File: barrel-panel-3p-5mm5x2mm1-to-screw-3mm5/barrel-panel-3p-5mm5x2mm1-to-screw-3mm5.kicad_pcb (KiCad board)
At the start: 2 copper layers, 1 part, among them J1 Barrel_Jack_Switch

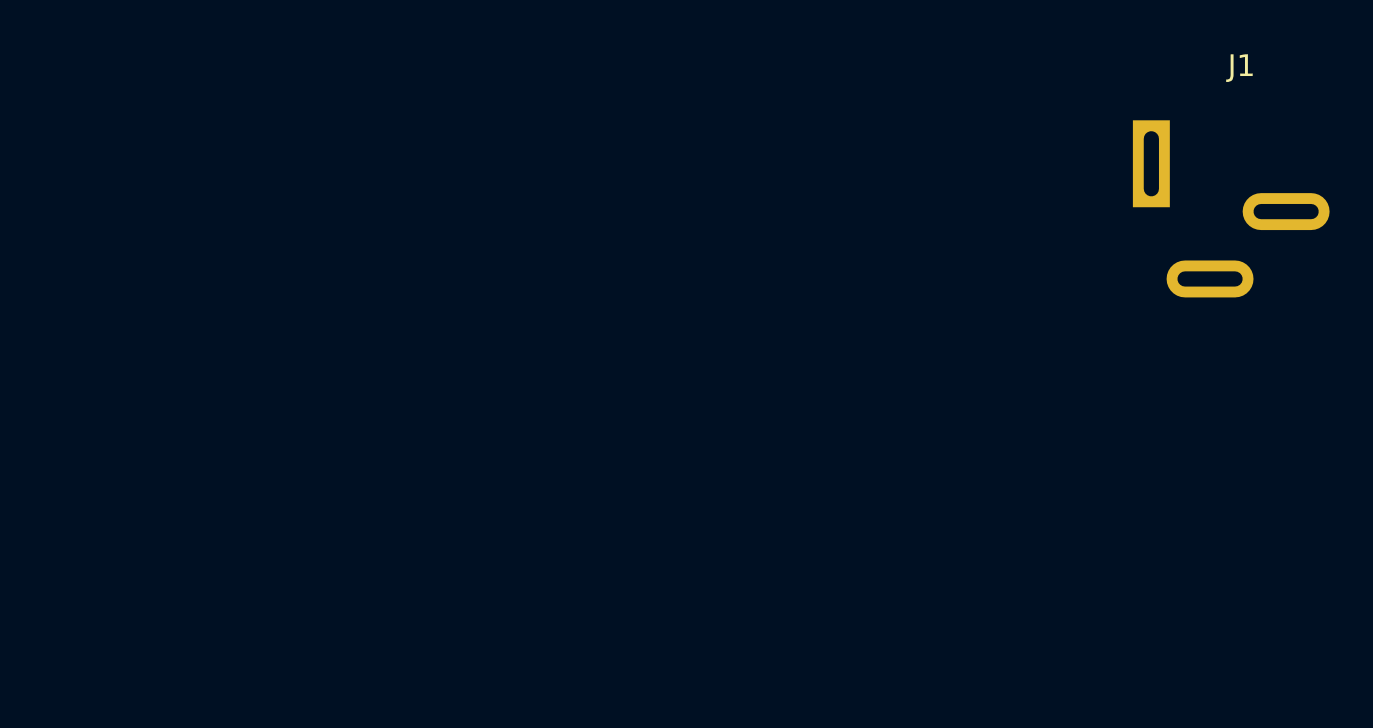
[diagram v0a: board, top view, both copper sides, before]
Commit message: footprint finished, all elements placed in board
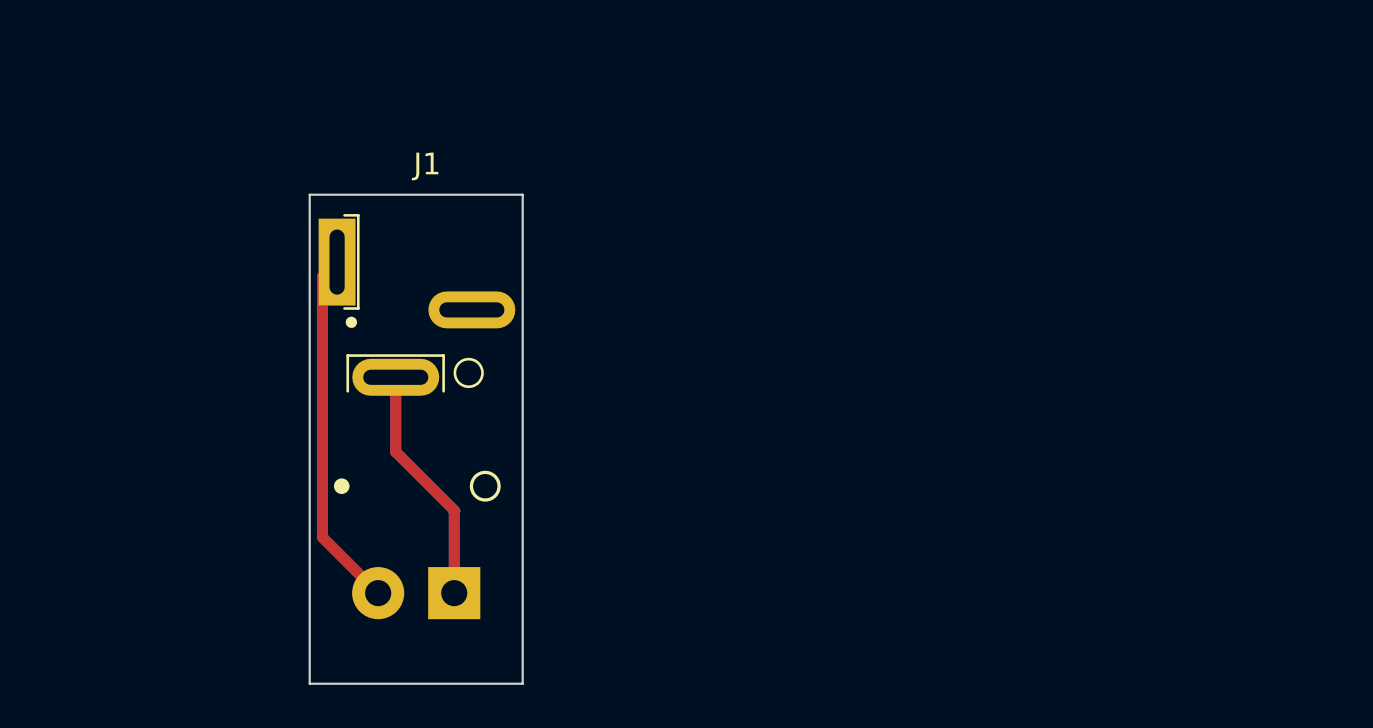
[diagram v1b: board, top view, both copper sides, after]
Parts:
- added J2: Conn_01x02_Male, TerminalBlock_4Ucon:TerminalBlock_4Ucon_1x02_P3.50mm_Horizontal, B.Cu at (106.7, 118.3)
- moved J1 37.7 mm to (105.4, 104.6)
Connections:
- J1 pad 1: unconnected-(J1-Pad1) -> Net-(J1-Pad1)
- J1 pad 2: unconnected-(J1-Pad2) -> Net-(J1-Pad2)
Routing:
- net Net-(J1-Pad1): track 0.00 -> 33.1 mm
- net Net-(J1-Pad2): track 0.00 -> 22.1 mm
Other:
- board outline added: 9.8 x 22.5 mm

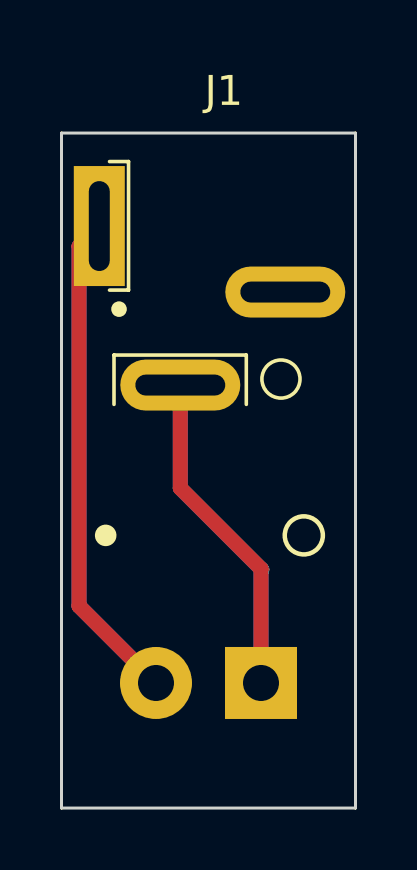
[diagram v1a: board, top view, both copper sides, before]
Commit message: shrinking pcb to let space for the nut
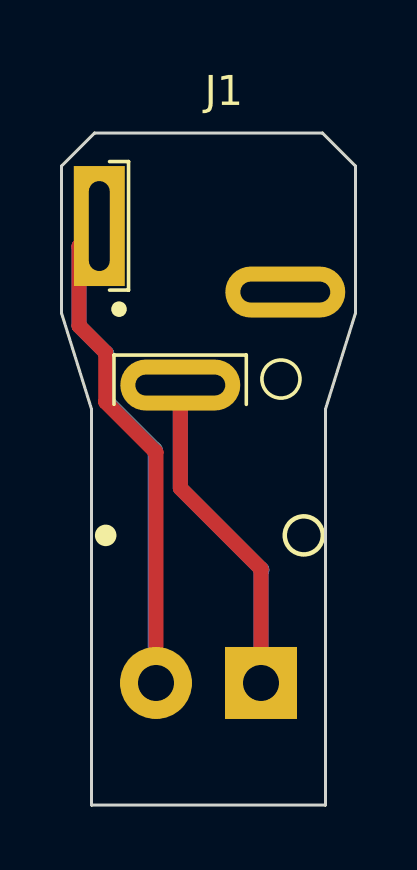
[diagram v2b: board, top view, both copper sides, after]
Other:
- board size 9.8 x 22.5 mm -> 9.8 x 22.4 mm
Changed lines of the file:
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@@
   (gr_circle (center 108.077 113.411) (end 108.585 113.03) (layer "F.SilkS") (width 0.15) (fill none))
   (gr_circle (center 101.473 113.411) (end 101.756981 113.411) (layer "F.SilkS") (width 0.15) (fill solid))
-  (gr_rect (start 100 100) (end 109.8 122.5) (layer "Edge.Cuts") (width 0.1) (fill none))
+  (gr_line (start 101.1 100) (end 108.7 100) (layer "Edge.Cuts") (width 0.1))
+  (gr_line (start 108.8 109.2) (end 109.8 106) (layer "Edge.Cuts") (width 0.1))
+  (gr_line (start 100 101.1) (end 100 106) (layer "Edge.Cuts") (width 0.1))
+  (gr_line (start 101 122.4) (end 108.8 122.4) (layer "Edge.Cuts") (width 0.1))
+  (gr_line (start 100 106) (end 101 109.2) (layer "Edge.Cuts") (width 0.1))
+  (gr_line (start 108.7 100) (end 109.8 101.1) (layer "Edge.Cuts") (width 0.1))
+  (gr_line (start 101.1 100) (end 100 101.1) (layer "Edge.Cuts") (width 0.1))
+  (gr_line (start 109.8 101.1) (end 109.8 106) (layer "Edge.Cuts") (width 0.1))
+  (gr_line (start 108.8 109.2) (end 108.8 122.4) (layer "Edge.Cuts") (width 0.1))
+  (gr_line (start 101 109.2) (end 101 122.4) (layer "Edge.Cuts") (width 0.1))
+  (segment (start 103.15 110.643) (end 103.15 118.331) (width 0.5) (layer "F.Cu") (net 1))
+  (segment (start 101.473 107.315) (end 101.473 108.966) (width 0.5) (layer "F.Cu") (net 1))
+  (segment (start 100.584 103.776) (end 100.584 106.426) (width 0.5) (layer "F.Cu") (net 1))
+  (segment (start 101.473 108.966) (end 103.15 110.643) (width 0.5) (layer "F.Cu") (net 1))
   (segment (start 101.26 103.1) (end 100.584 103.776) (width 0.5) (layer "F.Cu") (net 1))
-  (segment (start 100.584 103.776) (end 100.584 115.765) (width 0.5) (layer "F.Cu") (net 1))
-  (segment (start 100.584 115.765) (end 103.15 118.331) (width 0.5) (layer "F.Cu") (net 1))
-  (segment (start 100.584 115.765) (end 103.15 118.331) (width 0.5) (layer "B.Cu") (net 1))
-  (segment (start 100.584 103.776) (end 100.584 115.765) (width 0.5) (layer "B.Cu") (net 1))
-  (segment (start 100.584 103.776) (end 101.26 103.1) (width 0.5) (layer "B.Cu") (net 1))
+  (segment (start 100.584 106.426) (end 101.473 107.315) (width 0.5) (layer "F.Cu") (net 1))
+  (segment (start 101.51 108.938478) (end 103.124 110.552478) (width 0.5) (layer "B.Cu") (net 1))
+  (segment (start 100.584 106.426) (end 101.51 107.352) (width 0.5) (layer "B.Cu") (net 1))
+  (segment (start 101.51 107.352) (end 101.51 108.938478) (width 0.5) (layer "B.Cu") (net 1))
+  (segment (start 103.124 118.305) (end 103.15 118.331) (width 0.5) (layer "B.Cu") (net 1))
+  (segment (start 100.584 103.776) (end 100.584 106.426) (width 0.5) (layer "B.Cu") (net 1))
+  (segment (start 101.26 103.1) (end 100.584 103.776) (width 0.5) (layer "B.Cu") (net 1))
+  (segment (start 103.124 110.552478) (end 103.124 118.305) (width 0.5) (layer "B.Cu") (net 1))
   (segment (start 103.96 111.834) (end 106.65 114.524) (width 0.5) (layer "F.Cu") (net 2))
   (segment (start 103.96 108.4) (end 103.96 111.834) (width 0.5) (layer "F.Cu") (net 2))

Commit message: single board gerbers
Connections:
- J2 pad 1: Net-(J1-Pad2) -> Net-(J1-Pad1)
- J2 pad 2: Net-(J1-Pad1) -> Net-(J1-Pad2)
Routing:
- net Net-(J1-Pad1): track 33.1 -> 40.8 mm
- net Net-(J1-Pad2): track 22.1 -> 20.6 mm
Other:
- outline, holes or cut-outs redrawn
- board text added: "3.5 mm screw term"
- board text added: "DC BARREL 5.5x2.1mm"
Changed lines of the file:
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@@
       (sketchpadsonfab false)
       (subtractmaskfromsilk false)
-      (outputformat 5)
+      (outputformat 1)
       (mirror false)
-      (drillshape 2)
+      (drillshape 0)
       (scaleselection 1)
       (outputdirectory "gerber/single/")
@@
       (net 2 "Net-(J1-Pad2)") (pintype "passive"))
     (pad "3" thru_hole oval (at 2.05 0.7 90) (size 1.7 4) (drill oval 0.7 3) (layers *.Cu *.Mask)
-      (net 3 "unconnected-(J1-Pad3)") (pintype "passive"))
+      (net 3 "unconnected-(J1-Pad3)") (pintype "passive+no_connect"))
     (model "${KICAD6_3DMODEL_DIR}/Connector_BarrelJack.3dshapes/BarrelJack_Kycon_KLDX-0202-xC_Horizontal.wrl"
       (offset (xyz 0 0 0))
@@
     (property "Sheetname" "")
     (attr through_hole)
-    (fp_text reference "J2" (at 2.002 4.92) (layer "B.SilkS")
+    (fp_text reference "J2" (at 1.748 4.92) (layer "B.SilkS")
       (effects (font (size 1 1) (thickness 0.15)) (justify mirror))
     )
@@
     (fp_circle (center 3.5 0) (end 4.875 0) (layer "B.Fab") (width 0.1) (fill none))
     (pad "1" thru_hole rect (at 0 0 180) (size 2.4 2.4) (drill 1.2) (layers *.Cu *.Mask)
-      (net 2 "Net-(J1-Pad2)") (pinfunction "Pin_1") (pintype "passive"))
+      (net 1 "Net-(J1-Pad1)") (pinfunction "Pin_1") (pintype "passive"))
     (pad "2" thru_hole circle (at 3.5 0 180) (size 2.4 2.4) (drill 1.2) (layers *.Cu *.Mask)
-      (net 1 "Net-(J1-Pad1)") (pinfunction "Pin_2") (pintype "passive"))
+      (net 2 "Net-(J1-Pad2)") (pinfunction "Pin_2") (pintype "passive"))
     (model "${KICAD6_3DMODEL_DIR}/TerminalBlock_4Ucon.3dshapes/TerminalBlock_4Ucon_1x02_P3.50mm_Horizontal.wrl"
       (offset (xyz 0 0 0))
@@
     )
   )
-  (gr_circle (center 102.87 113.411) (end 103.153981 113.411) (layer "B.SilkS") (width 0.15) (fill solid))
-  (gr_circle (center 106.426 113.411) (end 107.061 113.411) (layer "B.SilkS") (width 0.15) (fill none))
-  (gr_circle (center 108.077 113.411) (end 108.585 113.03) (layer "F.SilkS") (width 0.15) (fill none))
-  (gr_circle (center 101.473 113.411) (end 101.756981 113.411) (layer "F.SilkS") (width 0.15) (fill solid))
-  (gr_line (start 101.1 100) (end 108.7 100) (layer "Edge.Cuts") (width 0.1))
-  (gr_line (start 108.8 109.2) (end 109.8 106) (layer "Edge.Cuts") (width 0.1))
+  (gr_circle (center 106.68 113.411) (end 106.963981 113.411) (layer "B.SilkS") (width 0.15) (fill solid))
+  (gr_circle (center 103.124 113.411) (end 103.759 113.411) (layer "B.SilkS") (width 0.15) (fill none))
+  (gr_circle (center 103.124 112.776) (end 103.632 112.395) (layer "F.SilkS") (width 0.15) (fill none))
+  (gr_circle (center 106.68 112.776) (end 106.963981 112.776) (layer "F.SilkS") (width 0.15) (fill solid))
+  (gr_line (start 101.1 100) (end 107.7 100) (layer "Edge.Cuts") (width 0.1))
+  (gr_line (start 108.2 107) (end 109.8 106) (layer "Edge.Cuts") (width 0.1))
   (gr_line (start 100 101.1) (end 100 106) (layer "Edge.Cuts") (width 0.1))
-  (gr_line (start 101 122.4) (end 108.8 122.4) (layer "Edge.Cuts") (width 0.1))
-  (gr_line (start 100 106) (end 101 109.2) (layer "Edge.Cuts") (width 0.1))
-  (gr_line (start 108.7 100) (end 109.8 101.1) (layer "Edge.Cuts") (width 0.1))
+  (gr_line (start 101.6 122.4) (end 108.2 122.4) (layer "Edge.Cuts") (width 0.1))
+  (gr_line (start 100 106) (end 101.6 107) (layer "Edge.Cuts") (width 0.1))
+  (gr_line (start 107.7 100) (end 109.8 102.1) (layer "Edge.Cuts") (width 0.1))
   (gr_line (start 101.1 100) (end 100 101.1) (layer "Edge.Cuts") (width 0.1))
-  (gr_line (start 109.8 101.1) (end 109.8 106) (layer "Edge.Cuts") (width 0.1))
-  (gr_line (start 108.8 109.2) (end 108.8 122.4) (layer "Edge.Cuts") (width 0.1))
-  (gr_line (start 101 109.2) (end 101 122.4) (layer "Edge.Cuts") (width 0.1))
-  (segment (start 103.15 110.643) (end 103.15 118.331) (width 0.5) (layer "F.Cu") (net 1))
-  (segment (start 101.473 107.315) (end 101.473 108.966) (width 0.5) (layer "F.Cu") (net 1))
-  (segment (start 100.584 103.776) (end 100.584 106.426) (width 0.5) (layer "F.Cu") (net 1))
-  (segment (start 101.473 108.966) (end 103.15 110.643) (width 0.5) (layer "F.Cu") (net 1))
+  (gr_line (start 109.8 102.1) (end 109.8 106) (layer "Edge.Cuts") (width 0.1))
+  (gr_line (start 108.2 107) (end 108.2 122.4) (layer "Edge.Cuts") (width 0.1))
+  (gr_line (start 101.6 107) (end 101.6 122.4) (layer "Edge.Cuts") (width 0.1))
+  (gr_text "DC BARREL\n5.5x2.1mm" (at 105.537 102.87) (layer "B.SilkS")
+    (effects (font (size 0.7 0.7) (thickness 0.175)) (justify mirror))
+  )
+  (gr_text "DC BARREL\n5.5x2.1mm" (at 105.664 101.854) (layer "F.SilkS")
+    (effects (font (size 0.7 0.7) (thickness 0.175)))
+  )
+  (gr_text "3.5 mm\nscrew term" (at 104.902 121.158) (layer "F.SilkS")
+    (effects (font (size 0.7 0.7) (thickness 0.175)))
+  )
+  (segment (start 102.616 105.537) (end 103.9495 105.537) (width 0.5) (layer "F.Cu") (net 1))
+  (segment (start 101.26 104.181) (end 102.616 105.537) (width 0.5) (layer "F.Cu") (net 1))
+  (segment (start 106.65 110.139) (end 106.65 118.331) (width 0.5) (layer "F.Cu") (net 1))
+  (segment (start 101.26 103.1) (end 101.26 104.181) (width 0.5) (layer "F.Cu") (net 1))
+  (segment (start 103.9495 105.537) (end 105.2195 106.807) (width 0.5) (layer "F.Cu") (net 1))
   (segment (start 101.26 103.1) (end 100.584 103.776) (width 0.5) (layer "F.Cu") (net 1))
-  (segment (start 100.584 106.426) (end 101.473 107.315) (width 0.5) (layer "F.Cu") (net 1))
-  (segment (start 101.51 108.938478) (end 103.124 110.552478) (width 0.5) (layer "B.Cu") (net 1))
-  (segment (start 100.584 106.426) (end 101.51 107.352) (width 0.5) (layer "B.Cu") (net 1))
-  (segment (start 101.51 107.352) (end 101.51 108.938478) (width 0.5) (layer "B.Cu") (net 1))
-  (segment (start 103.124 118.305) (end 103.15 118.331) (width 0.5) (layer "B.Cu") (net 1))
-  (segment (start 100.584 103.776) (end 100.584 106.426) (width 0.5) (layer "B.Cu") (net 1))
+  (segment (start 107.315 107.823) (end 107.315 109.474) (width 0.5) (layer "F.Cu") (net 1))
+  (segment (start 107.315 109.474) (end 106.65 110.139) (width 0.5) (layer "F.Cu") (net 1))
+  (segment (start 106.299 106.807) (end 107.315 107.823) (width 0.5) (layer "F.Cu") (net 1))
+  (segment (start 105.2195 106.807) (end 106.299 106.807) (width 0.5) (layer "F.Cu") (net 1))
+  (segment (start 106.65 118.331) (end 106.65 110.012) (width 0.5) (layer "B.Cu") (net 1))
+  (segment (start 101.26 104.181) (end 101.26 103.1) (width 0.5) (layer "B.Cu") (net 1))
+  (segment (start 105.2195 106.807) (end 103.9495 105.537) (width 0.5) (layer "B.Cu") (net 1))
+  (segment (start 103.9495 105.537) (end 102.616 105.537) (width 0.5) (layer "B.Cu") (net 1))
+  (segment (start 106.65 110.012) (end 107.315 109.347) (width 0.5) (layer "B.Cu") (net 1))
+  (segment (start 106.299 106.807) (end 105.2195 106.807) (width 0.5) (layer "B.Cu") (net 1))
+  (segment (start 107.315 109.347) (end 107.315 107.823) (width 0.5) (layer "B.Cu") (net 1))
+  (segment (start 102.616 105.537) (end 101.26 104.181) (width 0.5) (layer "B.Cu") (net 1))
+  (segment (start 107.315 107.823) (end 106.299 106.807) (width 0.5) (layer "B.Cu") (net 1))
   (segment (start 101.26 103.1) (end 100.584 103.776) (width 0.5) (layer "B.Cu") (net 1))
-  (segment (start 103.124 110.552478) (end 103.124 118.305) (width 0.5) (layer "B.Cu") (net 1))
-  (segment (start 103.96 111.834) (end 106.65 114.524) (width 0.5) (layer "F.Cu") (net 2))
-  (segment (start 103.96 108.4) (end 103.96 111.834) (width 0.5) (layer "F.Cu") (net 2))
-  (segment (start 106.65 114.524) (end 106.65 118.331) (width 0.5) (layer "F.Cu") (net 2))
-  (segment (start 106.68 114.554) (end 106.65 114.584) (width 0.5) (layer "B.Cu") (net 2))
-  (segment (start 103.96 108.4) (end 103.96 111.834) (width 0.5) (layer "B.Cu") (net 2))
-  (segment (start 103.96 111.834) (end 106.68 114.554) (width 0.5) (layer "B.Cu") (net 2))
-  (segment (start 106.65 114.584) (end 106.65 118.331) (width 0.5) (layer "B.Cu") (net 2))
+  (segment (start 103.15 109.21) (end 103.96 108.4) (width 0.5) (layer "F.Cu") (net 2))
+  (segment (start 103.15 118.331) (end 103.15 109.21) (width 0.5) (layer "F.Cu") (net 2))
+  (segment (start 103.15 109.21) (end 103.96 108.4) (width 0.5) (layer "B.Cu") (net 2))
+  (segment (start 103.124 118.305) (end 103.15 118.331) (width 0.5) (layer "B.Cu") (net 2))
+  (segment (start 103.15 118.331) (end 103.15 109.21) (width 0.5) (layer "B.Cu") (net 2))
 )
